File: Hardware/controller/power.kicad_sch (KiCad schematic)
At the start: 38 parts

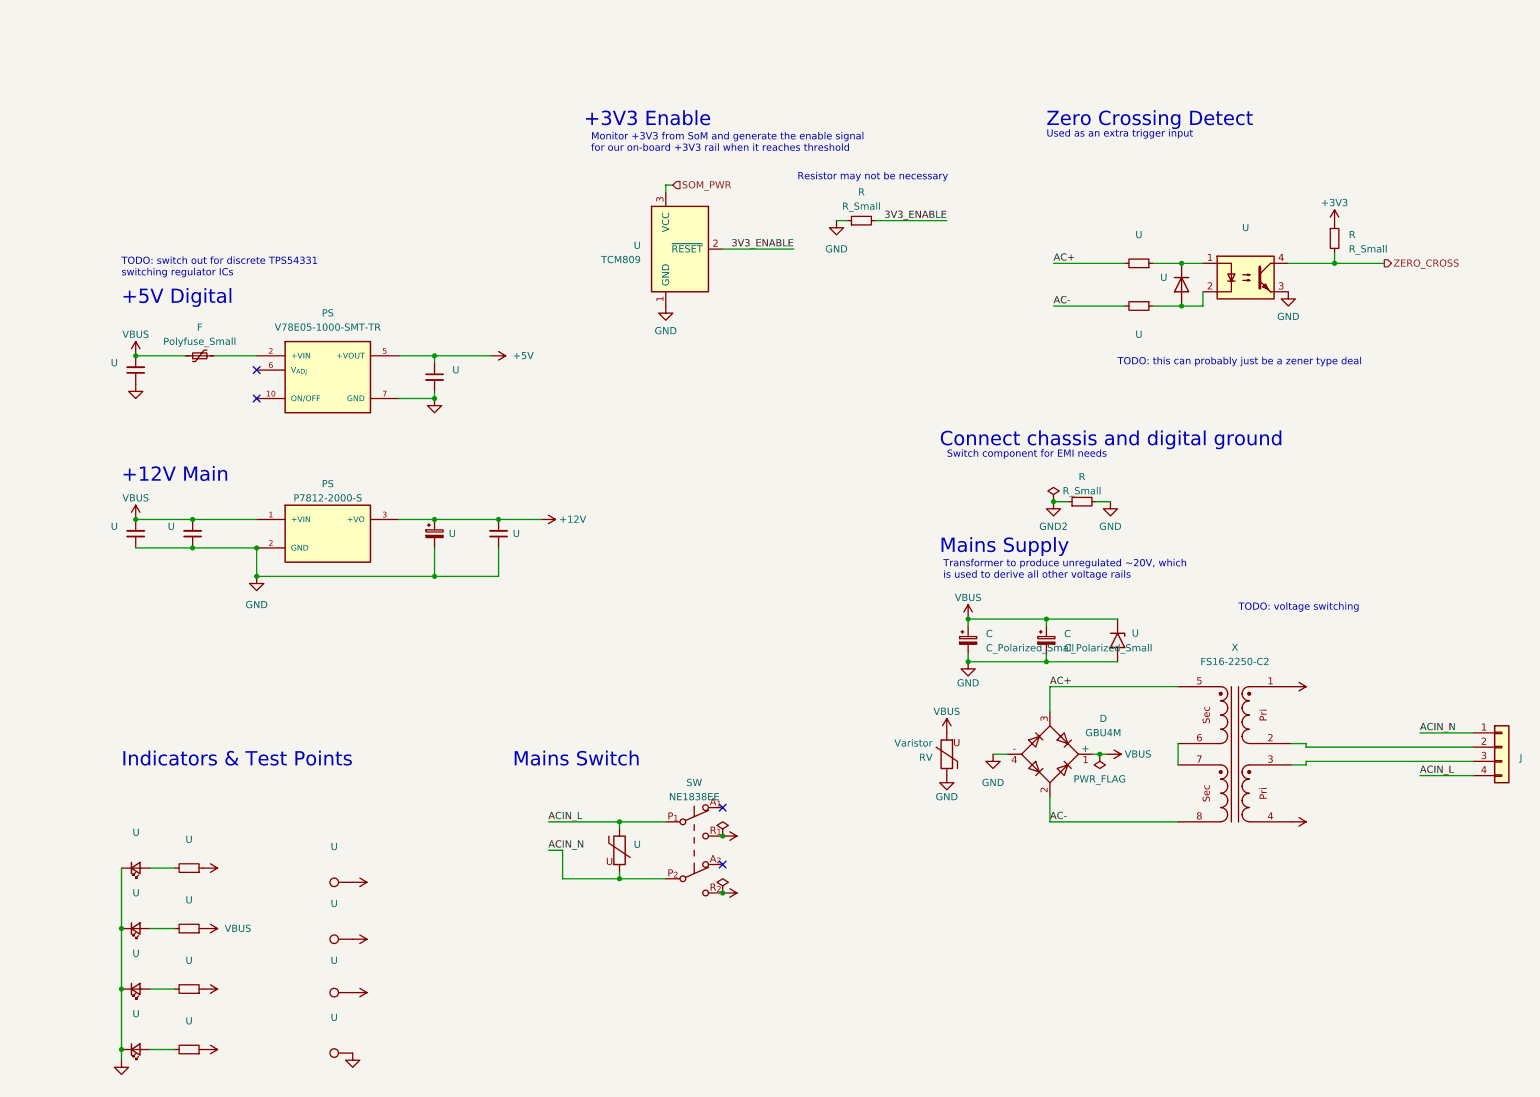
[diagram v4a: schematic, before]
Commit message: hw: start reworking power section
- replace the integrated power modules with a discrete power supply
  based around TPS54331 chip; so far this has been replaced for the +12V
  supply (complete with layout)

- added footprints for a few different inductors

- create footprint for TPS54331 DC/DC converter
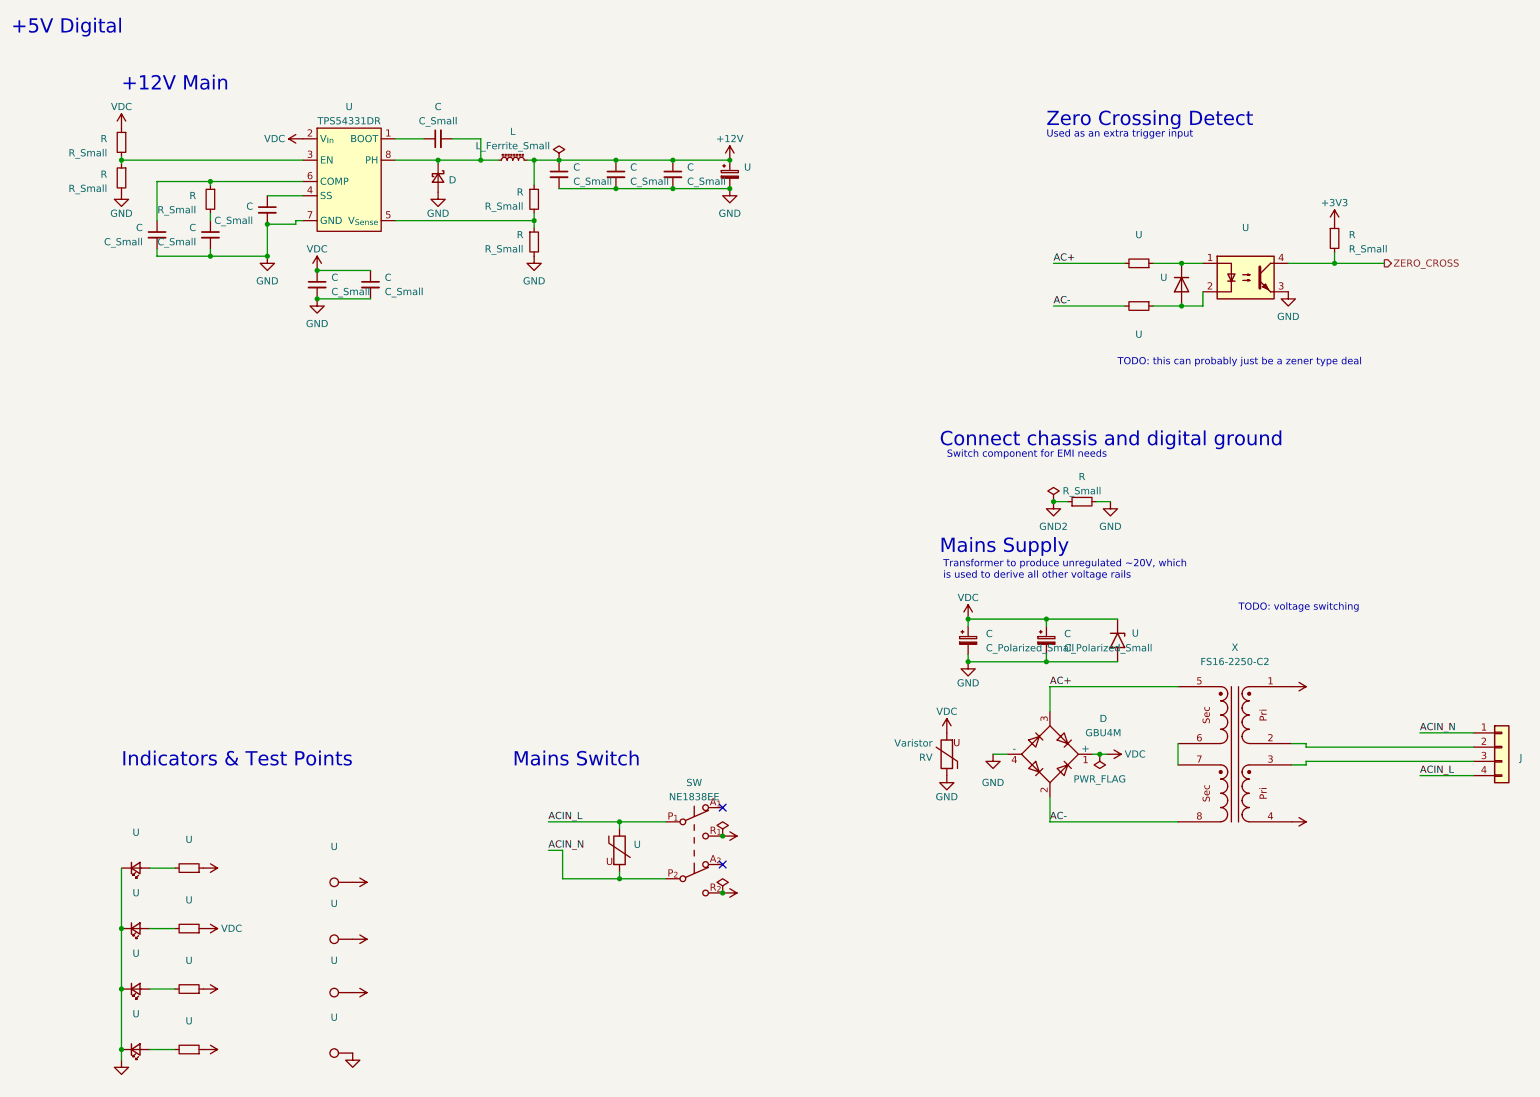
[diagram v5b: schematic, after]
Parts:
- removed F: Polyfuse_Small, symbol Device:Polyfuse_Small
- removed PS: V78E05-1000-SMT-TR, programmable-load:CONV_V78E03-1000-SMT-TR, symbol programmable-load:V78E05-1000-SMT-TR
- removed PS: P7812-2000-S, programmable-load:CONV_P7812-2000-S, symbol programmable-load:P7812-2000-S
- removed R: R_Small, symbol Device:R_Small
- removed U (x5): (no value), symbol Device:C_Small
- removed U: TCM809, symbol Power_Supervisor:TCM809
- added C (x9): C_Small, symbol Device:C_Small
- added D: D_Schottky_Small, symbol Device:D_Schottky_Small
- added L: L_Ferrite_Small, symbol Device:L_Ferrite_Small
- added R (x5): R_Small, symbol Device:R_Small
- added U: TPS54331DR, Package_SO:SOIC-8_3.9x4.9mm_P1.27mm, symbol programmable-load:TPS54331DR
- U: MPN A768EB336M1GLAE045 -> A750KK107M1EAAE040
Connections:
- net +12V: now also C.1, C.1, C.1, L.2, R.1
- net GND: now also C.2, C.2, C.2, C.2, C.2, C.2, C.2, C.2, D.2 (A), R.2, R.2, U.7 (GND)
- net VBUS renamed VDC
- net VDC: now also C.1, C.1, R.1, U.2 (V_{In})
- new net: C.1, U.1 (BOOT)
- new net: R.1, R.2, U.3 (EN)
- new net: C.1, U.4 (SS)
- new net: R.1, R.2, U.5 (V_{Sense})
- new net: C.1, R.1, U.6 (COMP)
- new net: C.2, D.1 (K), L.1, U.8 (PH)
- new net: C.1, R.2
- no-connect marks 4 -> 2
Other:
- note removed: "+3V3 Enable"
- note removed: "Monitor +3V3 from SoM and generate the enable signal for our on-board +3V3 rail when it reaches threshold"
- note removed: "Resistor may not be necessary"
- note removed: "TODO: switch out for discrete TPS54331 switching regulator ICs"

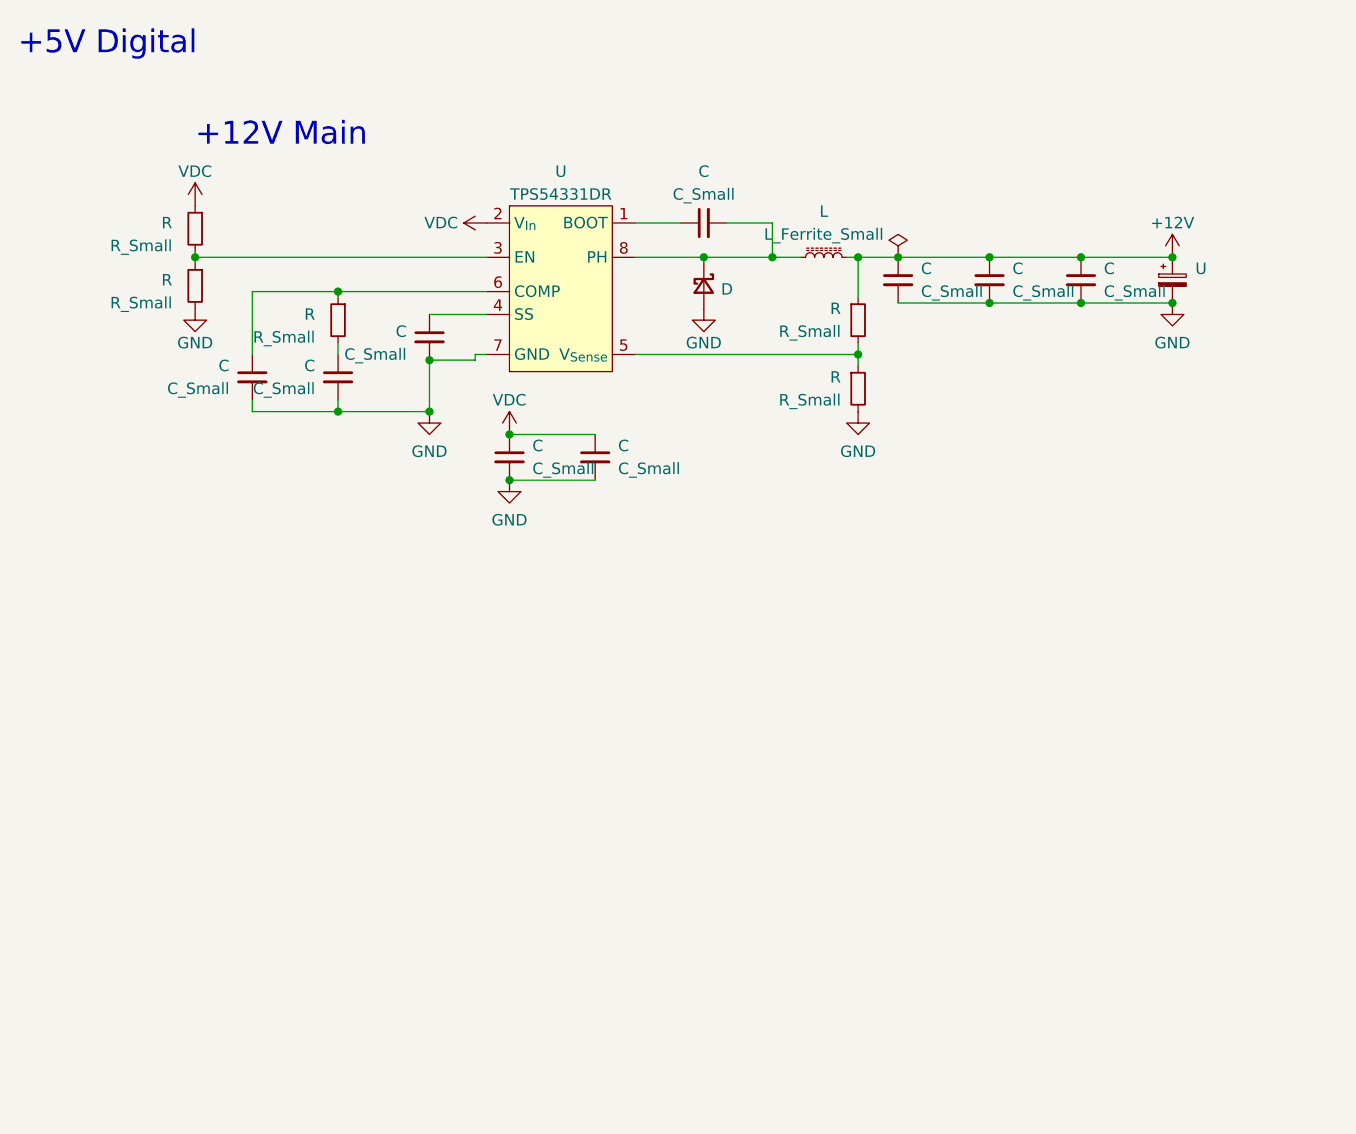
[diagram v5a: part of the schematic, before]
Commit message: hw: finish power section rework
- Changed the +5V supply to also use a new discrete regulator

- Moved fan controller to where the VBus LED is, so that the connector
  is easily accessible even with the analog board mounted in its card
  guides
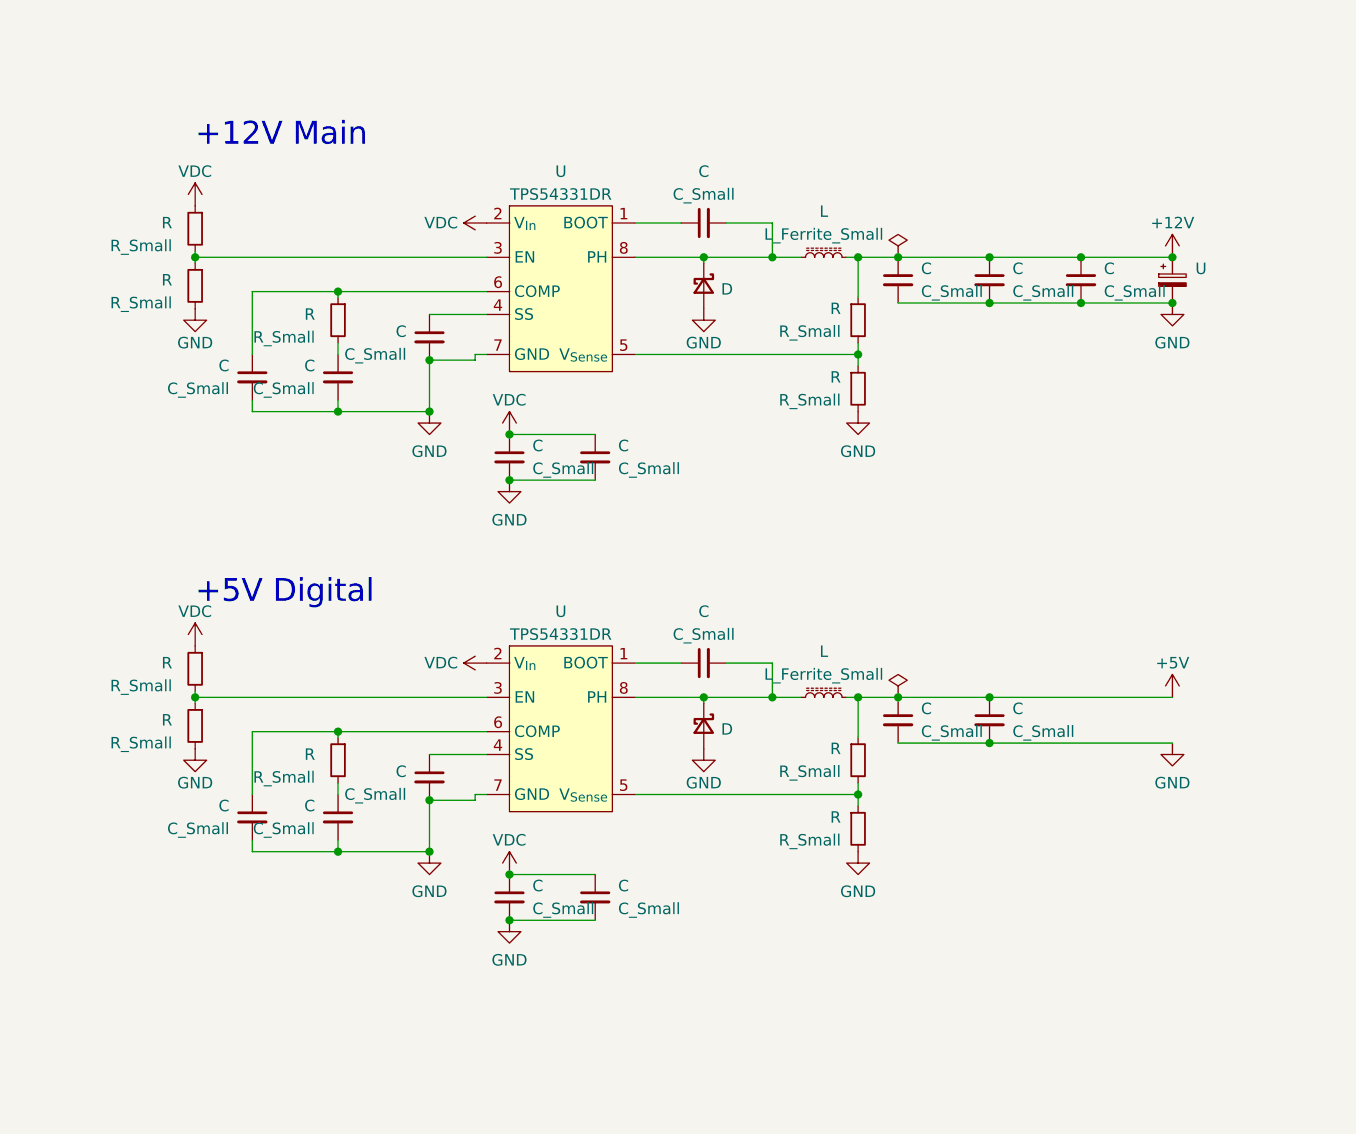
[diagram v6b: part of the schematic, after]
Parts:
- added C (x8): C_Small, symbol Device:C_Small
- added D: D_Schottky_Small, symbol Device:D_Schottky_Small
- added L: L_Ferrite_Small, symbol Device:L_Ferrite_Small
- added R (x5): R_Small, symbol Device:R_Small
- added U: TPS54331DR, Package_SO:SOIC-8_3.9x4.9mm_P1.27mm, symbol programmable-load:TPS54331DR
- D: MPN B340LA-13-F -> SS56-HF
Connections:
- net +5V: now also C.1, C.1, L.2, R.1
- net GND: now also C.2, C.2, C.2, C.2, C.2, C.2, C.2, D.2 (A), R.2, R.2, U.7 (GND)
- net VDC: now also C.1, C.1, R.1, U.2 (V_{In})
- new net: R.1, R.2, U.3 (EN)
- new net: C.1, U.1 (BOOT)
- new net: C.2, D.1 (K), L.1, U.8 (PH)
- new net: C.1, U.4 (SS)
- new net: C.1, R.1, U.6 (COMP)
- new net: C.1, R.2
- new net: R.1, R.2, U.5 (V_{Sense})

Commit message: hw: add more jlcpcb p/n; minor cleanup
- added jlcpcb part numbers for various resistors and passives

- minor clean up of stuff on the board, including moving the +VDC
  indicator LED and widening the fastener slot for the RTC supercap
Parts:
- R, U: JLCPCB (none) -> C23162
- U: JLCPCB (none) -> C4190
- U: JLCPCB (none) -> C25804
- U: JLCPCB (none) -> C23234
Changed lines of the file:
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@@
+      (effects (font (size 1.27 1.27)) hide)
+    )
+    (property "JLCPCB" "C4190" (id 5) (at 37.465 189.865 90)
       (effects (font (size 1.27 1.27)) hide)
     )
@@
     )
     (property "MPN" "" (id 4) (at 37.465 168.275 90)
+      (effects (font (size 1.27 1.27)) hide)
+    )
+    (property "JLCPCB" "C25804" (id 5) (at 37.465 168.275 90)
       (effects (font (size 1.27 1.27)) hide)
     )
@@
       (effects (font (size 1.27 1.27)) hide)
     )
+    (property "JLCPCB" "C23234" (id 5) (at 207.01 49.53 90)
+      (effects (font (size 1.27 1.27)) hide)
+    )
     (pin "1")
     (pin "2")
@@
       (effects (font (size 1.27 1.27)) hide)
     )
+    (property "JLCPCB" "C23234" (id 5) (at 37.465 157.48 90)
+      (effects (font (size 1.27 1.27)) hide)
+    )
     (pin "1")
     (pin "2")
@@
       (effects (font (size 1.27 1.27)) hide)
     )
+    (property "JLCPCB" "C23162" (id 5) (at 37.465 179.07 90)
+      (effects (font (size 1.27 1.27)) hide)
+    )
     (pin "1")
     (pin "2")
@@
     )
     (property "MPN" "" (id 4) (at 207.01 57.15 90)
+      (effects (font (size 1.27 1.27)) hide)
+    )
+    (property "JLCPCB" "C23234" (id 5) (at 207.01 57.15 90)
       (effects (font (size 1.27 1.27)) hide)
     )
@@
       (effects (font (size 1.27 1.27)) hide)
     )
+    (property "JLCPCB" "C23162" (id 4) (at 241.935 45.085 0)
+      (effects (font (size 1.27 1.27)) hide)
+    )

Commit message: hw: add more part numbers, cleanup
- Added JLCPCB part numbers for more passive components

- Added a status LED for the rear of the board (next to the device USB
  port)
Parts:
- C: JLCPCB (none) -> C57112
- C: JLCPCB (none) -> C1634
- C: JLCPCB (none) -> C1588
- U: JLCPCB (none) -> C2297
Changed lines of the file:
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@@
+      (effects (font (size 1.27 1.27)) hide)
+    )
+    (property "JLCPCB" "C2297" (id 5) (at 27.94 189.865 0)
       (effects (font (size 1.27 1.27)) hide)
     )
@@
       (effects (font (size 1.27 1.27)) hide)
     )
+    (property "JLCPCB" "C2297" (id 5) (at 27.94 179.07 0)
+      (effects (font (size 1.27 1.27)) hide)
+    )
     (pin "1")
     (pin "2")
@@
     )
     (property "Datasheet" "~" (id 3) (at 51.435 88.9 0)
+      (effects (font (size 1.27 1.27)) hide)
+    )
+    (property "JLCPCB" "C57112" (id 4) (at 51.435 88.9 0)
       (effects (font (size 1.27 1.27)) hide)
     )
@@
     )
     (property "Datasheet" "~" (id 3) (at 31.75 93.345 0)
+      (effects (font (size 1.27 1.27)) hide)
+    )
+    (property "JLCPCB" "C1634" (id 4) (at 31.75 93.345 0)
       (effects (font (size 1.27 1.27)) hide)
     )
@@
       (effects (font (size 1.27 1.27)) hide)
     )
+    (property "JLCPCB" "C2297" (id 5) (at 27.94 168.275 0)
+      (effects (font (size 1.27 1.27)) hide)
+    )
     (pin "1")
     (pin "2")
@@
     )
     (property "MPN" "150080VS75000" (id 4) (at 27.94 157.48 0)
+      (effects (font (size 1.27 1.27)) hide)
+    )
+    (property "JLCPCB" "C2297" (id 5) (at 27.94 157.48 0)
       (effects (font (size 1.27 1.27)) hide)
     )
@@
       (effects (font (size 1.27 1.27)) hide)
     )
+    (property "JLCPCB" "C57112" (id 4) (at 51.435 40.005 0)
+      (effects (font (size 1.27 1.27)) hide)
+    )
     (pin "1")
     (pin "2")
@@
     )
     (property "Datasheet" "~" (id 3) (at 31.75 44.45 0)
+      (effects (font (size 1.27 1.27)) hide)
+    )
+    (property "JLCPCB" "C1634" (id 4) (at 31.75 44.45 0)
       (effects (font (size 1.27 1.27)) hide)
     )
@@
       (effects (font (size 1.27 1.27)) hide)
     )
+    (property "JLCPCB" "C1588" (id 4) (at 41.275 93.345 0)
+      (effects (font (size 1.27 1.27)) hide)
+    )
     (pin "1")
     (pin "2")
@@
       (effects (font (size 1.27 1.27)) hide)
     )
+    (property "JLCPCB" "C1588" (id 4) (at 41.275 44.45 0)
+      (effects (font (size 1.27 1.27)) hide)
+    )
